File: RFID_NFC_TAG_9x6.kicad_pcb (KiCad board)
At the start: 2 copper layers, 9 x 6.6 mm, 3 parts, among them U1 SL2S2602FTBX

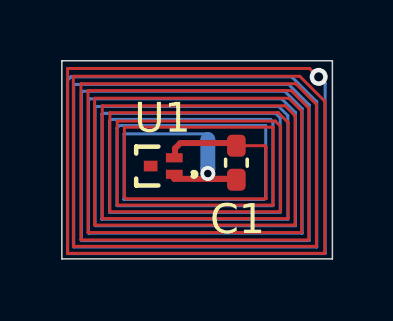
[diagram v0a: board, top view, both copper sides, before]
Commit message: Tidy up of trace spacing. Added larger pads to NFC chip.
Initial design had irregular spacing between traces on top and bottom layer. With this revision the lower copper was used for the spacing on the top layer, and vice versa. In this way a very even track spacing was achieved which cut down on overall size of PCB fractionally.
From the first batch initial success was achieved on 20 of 24 tags. Of the remaining 4 2 were fixed by touching solder to the caps.
The remaining issues were with the NXP chip where I could not get heat to bottom for reheat soldering. Slightly larger pads were added wxtending out from under the IC outline which will also allow accepting a little more solder paste.
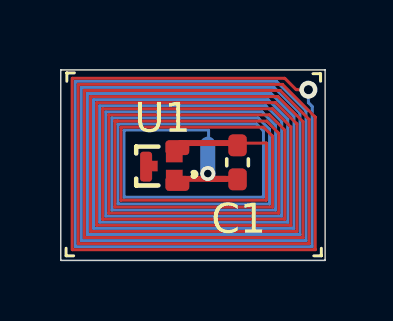
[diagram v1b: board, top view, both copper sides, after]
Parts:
- removed NT1: Ant Conn 1, NetTie:NetTie-2_SMD_Pad0.5mm
- added ?: , , F.Cu at (130.1, 73.7)
- added ?: , , F.Cu at (131.2, 74.2)
- added ?: , , F.Cu at (131.2, 73.1)
- added REF**: NetTie-2_SMD_Pad0.5mm, NetTie:NetTie-2_SMD_Pad0.5mm, B.Cu at (132.2, 73.4)
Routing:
- net ANT_LA: track 385.1 -> 368.1 mm
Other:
- board size 9 x 6.6 mm -> 8.8 x 6.4 mm
- board text added: "RFID R1a"
